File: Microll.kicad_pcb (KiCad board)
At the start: 2 copper layers, 5 parts, among them J1 USB_C_Receptacle, U1 AP7173-FNG-7, U2 STM32G0B1CBU6, U3 ESP32-C3-WROOM-02-N4, U4 LSM6DSL

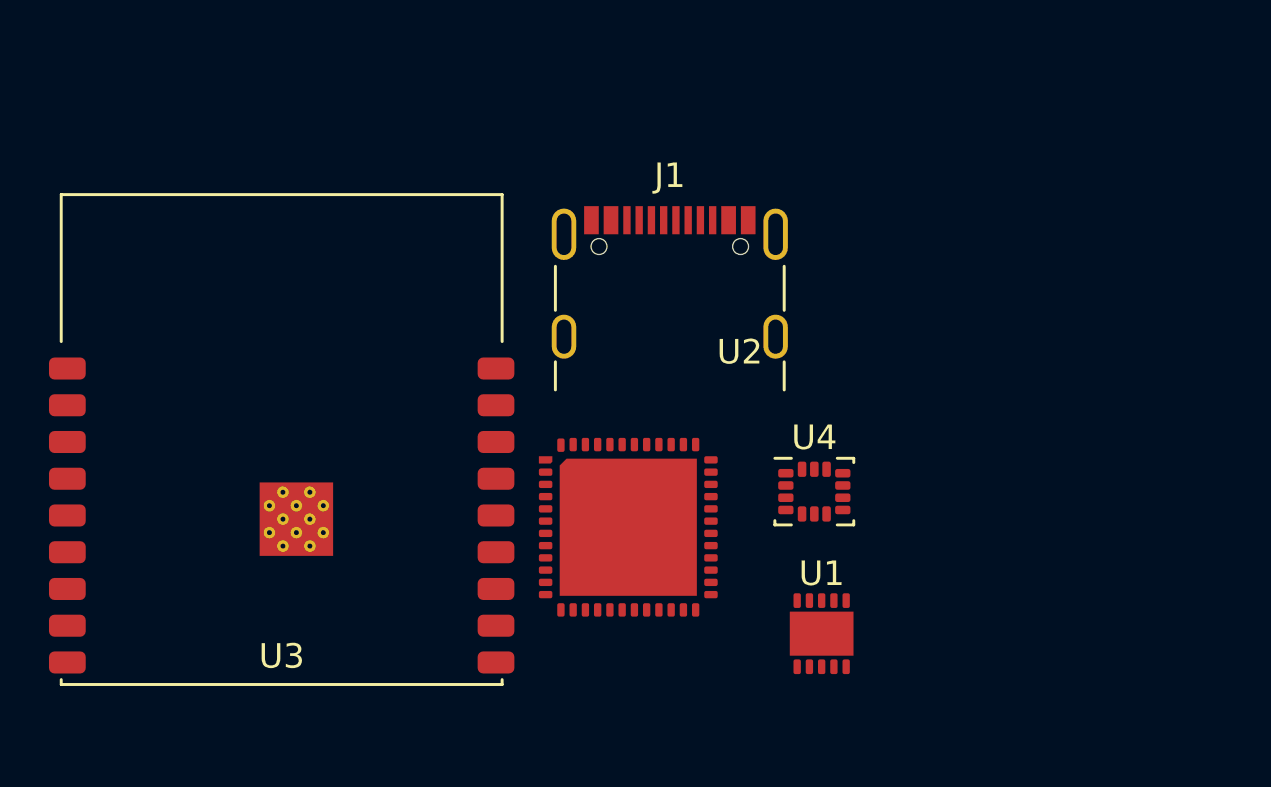
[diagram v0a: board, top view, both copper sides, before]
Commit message: Added 3D models to all PCB components. Added switch for USB programming between microcontrollers
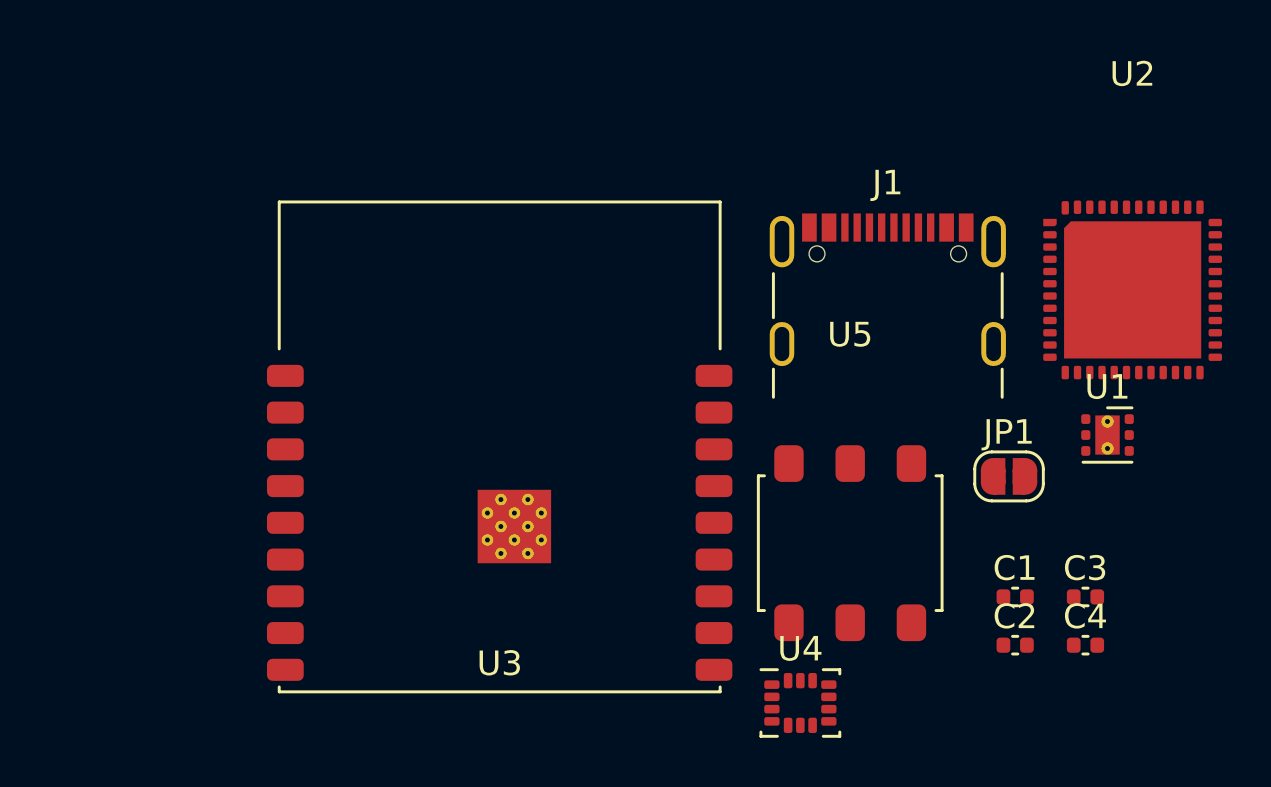
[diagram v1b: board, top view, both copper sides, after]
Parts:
- added C1: 1uF, Capacitor_SMD:C_0402_1005Metric, F.Cu at (159.2, 94.4)
- added C2: 1uF, Capacitor_SMD:C_0402_1005Metric, F.Cu at (159.2, 96.4)
- added C3: 100nF, Capacitor_SMD:C_0402_1005Metric, F.Cu at (162.1, 94.4)
- added C4: 100nF, Capacitor_SMD:C_0402_1005Metric, F.Cu at (162.1, 96.4)
- added JP1: SolderJumper_2_Open, Jumper:SolderJumper-2_P1.3mm_Open_RoundedPad1.0x1.5mm, F.Cu at (158.9, 89.5)
- added U5: DPDT_Switch_x2, DPDT_Switch_x2:DPDT_Switch_x2, F.Cu at (152.5, 92.2)
- U1: value AP7173-FNG-7 -> TLV76733DRVx; footprint AP7173-FNG-7:AP7173-FNG-7 -> Package_SON:WSON-6-1EP_2x2mm_P0.65mm_EP1x1.6mm_ThermalVias
- moved U2 17.5 mm to (164.0, 81.9)
- moved U1 14.2 mm to (163.0, 87.8)
- moved J1 8.91 mm to (154.0, 83.0)
- moved U3 8.91 mm to (138.2, 91.4)
- moved U4 8.65 mm to (150.4, 98.7)
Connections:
- J1 pad A1: Net-(J1-PadA1) -> GND
- J1 pad A12: Net-(J1-PadA1) -> GND
- J1 pad A4: Net-(J1-PadA4) -> +5V
- J1 pad A6: unconnected-(J1-PadA6) -> Net-(J1-PadA6)
- J1 pad A7: unconnected-(J1-PadA7) -> Net-(J1-PadA7)
- J1 pad A9: Net-(J1-PadA4) -> +5V
- J1 pad B1: Net-(J1-PadA1) -> GND
- J1 pad B12: Net-(J1-PadA1) -> GND
- J1 pad B4: Net-(J1-PadA4) -> +5V
- J1 pad B6: unconnected-(J1-PadB6) -> Net-(J1-PadA6)
- J1 pad B7: unconnected-(J1-PadB7) -> Net-(J1-PadA7)
- J1 pad B9: Net-(J1-PadA4) -> +5V
- U1 pad 1: unconnected-(U1-Pad1) -> +3.3V
- U1 pad 2: unconnected-(U1-Pad2) -> Net-(C2-Pad2)
- U1 pad 3: unconnected-(U1-Pad3) -> Net-(C1-Pad2)
- U1 pad 4: unconnected-(U1-Pad4) -> +5V
- U1 pad 5: unconnected-(U1-Pad5) -> Net-(C1-Pad2)
- U1 pad 6: unconnected-(U1-Pad6) -> +5V
- U1 pad 7: unconnected-(U1-Pad7) -> Net-(C1-Pad2)
- U2 pad 33: unconnected-(U2-Pad33) -> /STM32_USB-
- U2 pad 34: unconnected-(U2-Pad34) -> /STM32_USB+
- U3 pad 13: unconnected-(U3-Pad13) -> /ESP32_USB-
- U3 pad 14: unconnected-(U3-Pad14) -> /ESP32_USB+
- U4 pad 5: unconnected-(U4-Pad5) -> Net-(U4-Pad5)
- U4 pad 6: unconnected-(U4-Pad6) -> GND
- U4 pad 7: unconnected-(U4-Pad7) -> GND
- U4 pad 8: unconnected-(U4-Pad8) -> Net-(U4-Pad8)

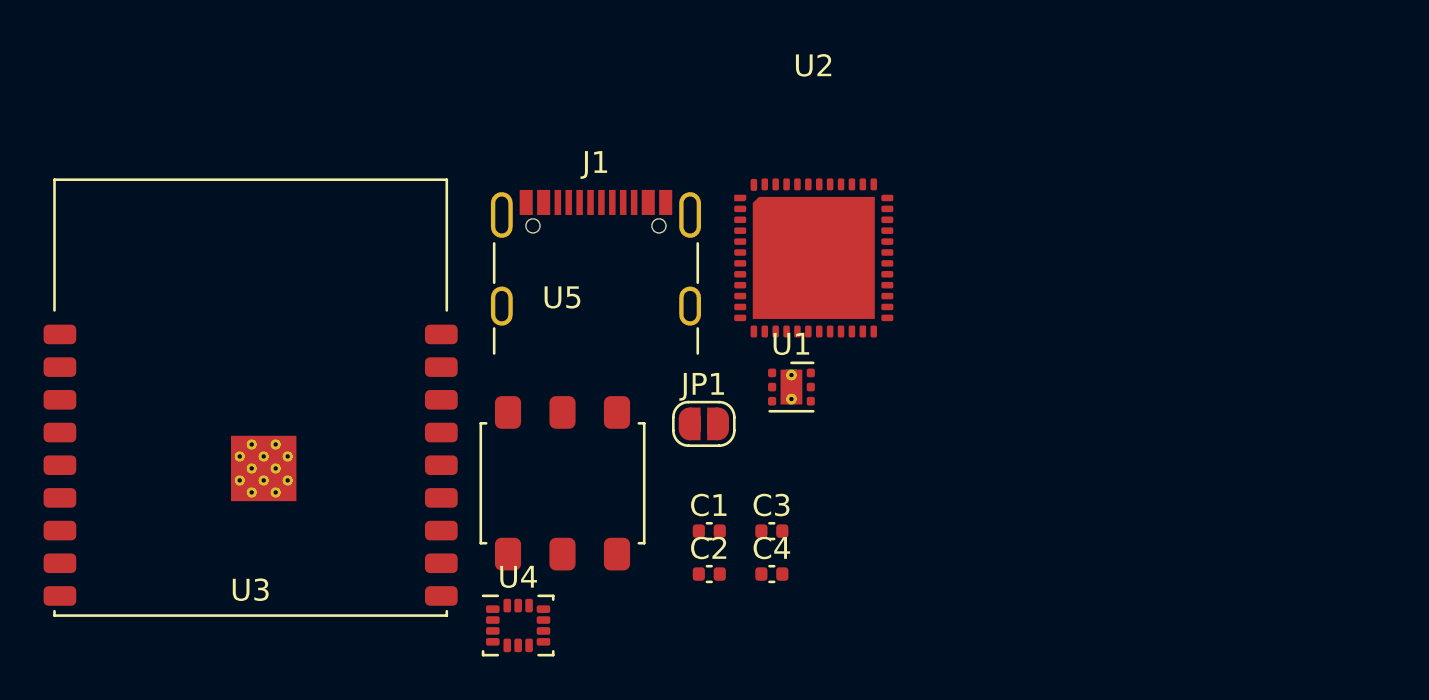
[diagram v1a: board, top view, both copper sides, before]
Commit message: Added ESD protection, decoupling capacitors and new footprints
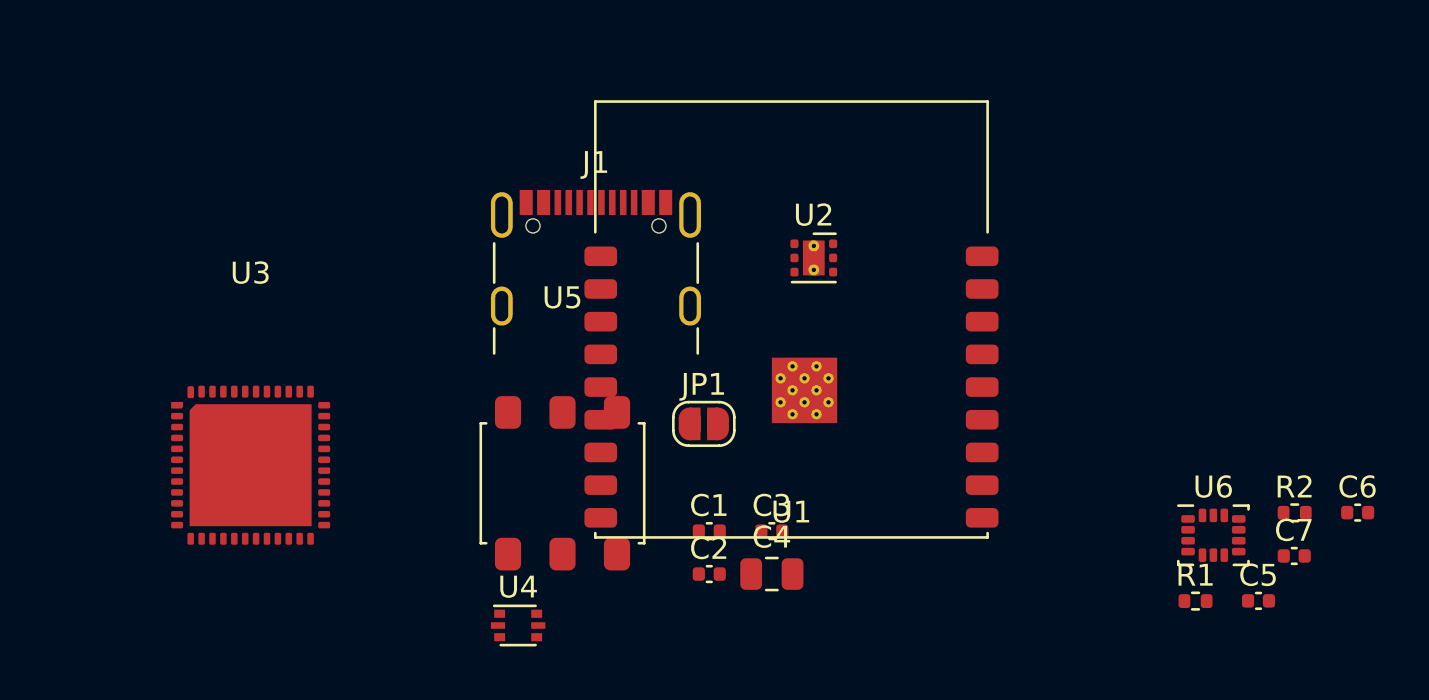
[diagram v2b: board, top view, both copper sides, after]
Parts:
- added C5: 100nF, Capacitor_SMD:C_0402_1005Metric, F.Cu at (184.4, 97.6)
- added C6: 100nF, Capacitor_SMD:C_0402_1005Metric, F.Cu at (188.9, 93.5)
- added C7: 100nF, Capacitor_SMD:C_0402_1005Metric, F.Cu at (186.0, 95.5)
- added R1: 10k, Resistor_SMD:R_0402_1005Metric, F.Cu at (181.5, 97.6)
- added R2: 10k, Resistor_SMD:R_0402_1005Metric, F.Cu at (186.1, 93.6)
- added U6: LSM6DSL, Package_LGA:LGA-14_3x2.5mm_P0.5mm_LayoutBorder3x4y, F.Cu at (182.3, 94.6)
- C4: value 100nF -> 4.7uF; footprint Capacitor_SMD:C_0402_1005Metric -> Capacitor_SMD:C_0805_2012Metric
- U1: value TLV76733DRVx -> ESP32-C3-WROOM-02-N4; footprint Package_SON:WSON-6-1EP_2x2mm_P0.65mm_EP1x1.6mm_ThermalVias -> ESP32:ESP32-C3-WROOM-02-N4
- U2: value STM32G0B1CBU6 -> TLV76733DRVx; footprint STM32:STM32G0B1CBU6 -> Package_SON:WSON-6-1EP_2x2mm_P0.65mm_EP1x1.6mm_ThermalVias
- U3: value ESP32-C3-WROOM-02-N4 -> STM32G0B1CBU6; footprint ESP32:ESP32-C3-WROOM-02-N4 -> STM32:STM32G0B1CBU6
- U4: value LSM6DSL -> USBLC6-2P6; footprint Package_LGA:LGA-14_3x2.5mm_P0.5mm_LayoutBorder3x4y -> Package_TO_SOT_SMD:SOT-666
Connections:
- C1 pad 2: Net-(C1-Pad2) -> GND
- C3 pad 1: Net-(U4-Pad5) -> +3.3V
- C4 pad 1: Net-(U4-Pad8) -> +3.3V
- J1 pad A6: Net-(J1-PadA6) -> /D+
- J1 pad A7: Net-(J1-PadA7) -> /D-
- J1 pad B6: Net-(J1-PadA6) -> /D+
- J1 pad B7: Net-(J1-PadA7) -> /D-
- U1 pad 2: Net-(C2-Pad2) -> unconnected-(U1-Pad2)
- U1 pad 3: Net-(C1-Pad2) -> (no net)
- U1 pad 4: +5V -> SCL
- U1 pad 5: Net-(C1-Pad2) -> unconnected-(U1-Pad5)
- U1 pad 6: +5V -> unconnected-(U1-Pad6)
- U1 pad 7: Net-(C1-Pad2) -> unconnected-(U1-Pad7)
- U2 pad 1: unconnected-(U2-Pad1) -> +3.3V
- U2 pad 2: unconnected-(U2-Pad2) -> Net-(C2-Pad2)
- U2 pad 3: unconnected-(U2-Pad3) -> GND
- U2 pad 4: unconnected-(U2-Pad4) -> +5V
- U2 pad 5: unconnected-(U2-Pad5) -> GND
- U2 pad 6: unconnected-(U2-Pad6) -> +5V
- U2 pad 7: unconnected-(U2-Pad7) -> GND
- U3 pad 11: unconnected-(U3-Pad11) -> /ADC1_IN0
- U3 pad 12: unconnected-(U3-Pad12) -> /ADC1_IN1
- U3 pad 13: /ESP32_USB- -> unconnected-(U3-Pad13)
- U3 pad 14: /ESP32_USB+ -> unconnected-(U3-Pad14)
- U3 pad 15: unconnected-(U3-Pad15) -> /DAC1_OUT1
- U3 pad 16: unconnected-(U3-Pad16) -> SPI_SCK
- U3 pad 17: unconnected-(U3-Pad17) -> SPI_MISO
- U3 pad 18: unconnected-(U3-Pad18) -> SPI_MOSI
- U3 pad 3: (no net) -> unconnected-(U3-Pad3)
- U3 pad 5: unconnected-(U3-Pad5) -> +3.3V
- U3 pad 6: unconnected-(U3-Pad6) -> +3.3V
- U3 pad 7: unconnected-(U3-Pad7) -> GND
- U4 pad 1: unconnected-(U4-Pad1) -> /USB-
- U4 pad 2: unconnected-(U4-Pad2) -> GND
- U4 pad 3: unconnected-(U4-Pad3) -> /USB+
- U4 pad 4: unconnected-(U4-Pad4) -> /D+
- U4 pad 5: Net-(U4-Pad5) -> +5V
- U4 pad 6: GND -> /D-
- U5 pad 1: /STM32_USB+ -> STM32_USB+
- U5 pad 2: Net-(J1-PadA7) -> /USB+
- U5 pad 3: /STM32_USB- -> ESP32_USB+
- U5 pad 4: /ESP32_USB+ -> STM32_USB-
- U5 pad 5: Net-(J1-PadA6) -> /USB-
- U5 pad 6: /ESP32_USB- -> ESP32_USB-

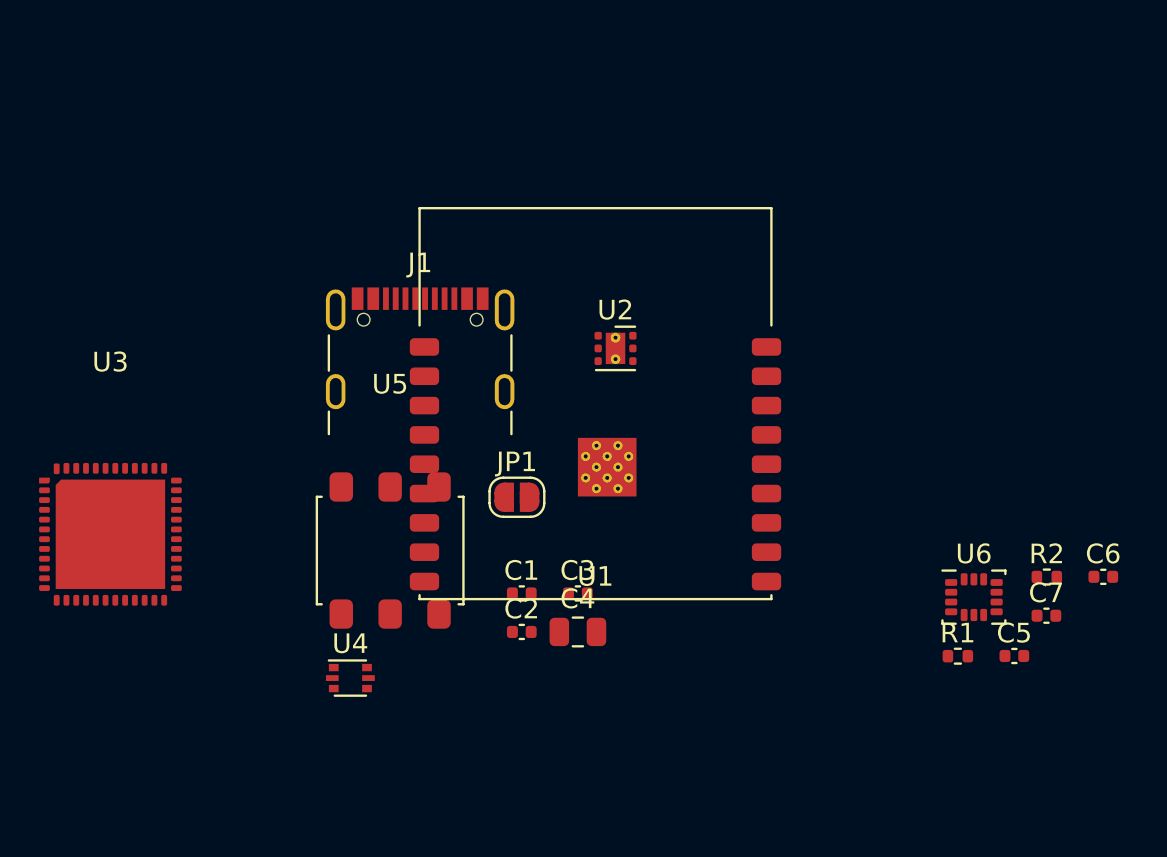
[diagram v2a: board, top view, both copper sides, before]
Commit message: Added nets to the LEDs. Pretty much all that is left in the scematic is adding the I/O pins and then it's off to the PCB layout
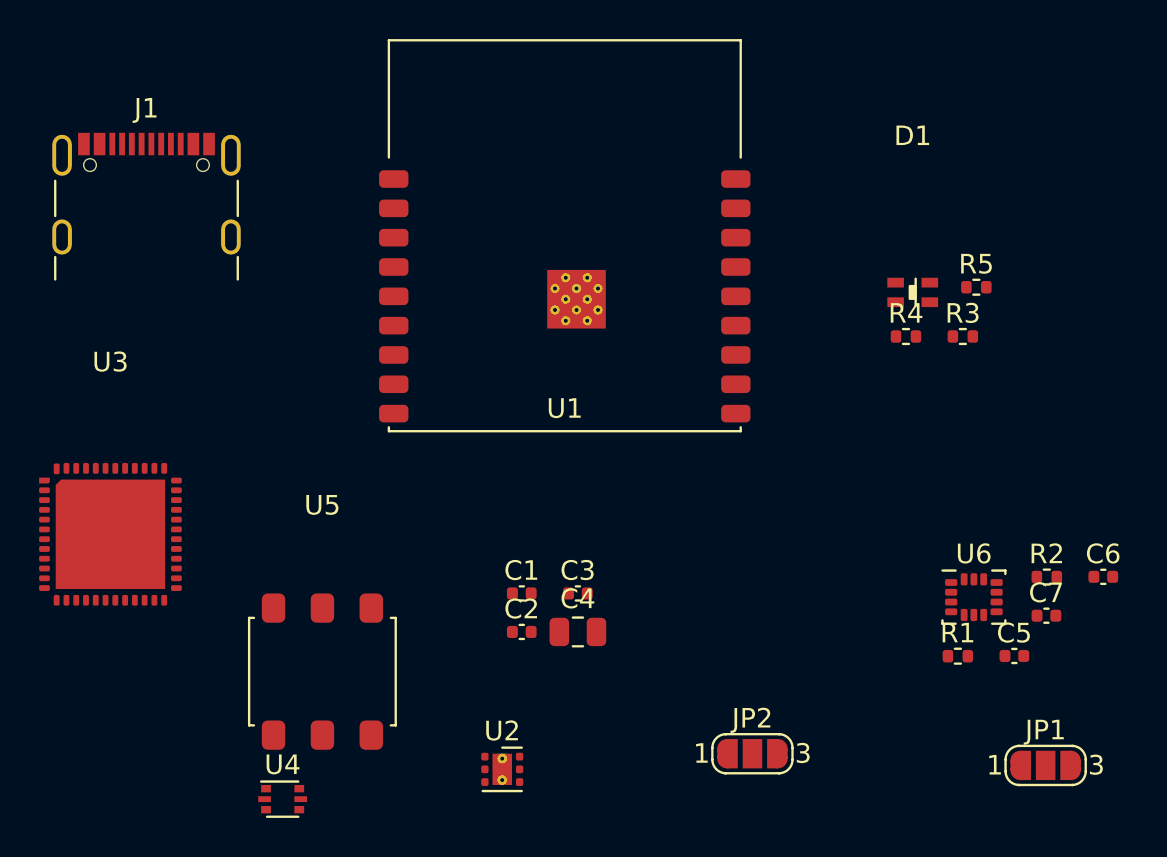
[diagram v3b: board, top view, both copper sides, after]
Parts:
- added D1: LED_ARGB, RGB_LED:APTF1616LSEEZGKQBKC, F.Cu at (179.2, 79.0)
- added JP2: SolderJumper_3_Open, Jumper:SolderJumper-3_P1.3mm_Open_RoundedPad1.0x1.5mm_NumberLabels, F.Cu at (171.0, 102.6)
- added R3: 10k, Resistor_SMD:R_0402_1005Metric, F.Cu at (181.8, 81.3)
- added R4: 10k, Resistor_SMD:R_0402_1005Metric, F.Cu at (178.9, 81.3)
- added R5: 10k, Resistor_SMD:R_0402_1005Metric, F.Cu at (182.5, 78.7)
- JP1: value SolderJumper_2_Open -> SolderJumper_3_Open; footprint Jumper:SolderJumper-2_P1.3mm_Open_RoundedPad1.0x1.5mm -> Jumper:SolderJumper-3_P1.3mm_Open_RoundedPad1.0x1.5mm_NumberLabels
- moved JP1 30.3 mm to (186.0, 103.2)
- moved U2 22.3 mm to (158.2, 103.4)
- moved J1 16.1 mm to (140.0, 75.1)
- moved U1 8.73 mm to (161.4, 79.2)
- moved U5 7.10 mm to (149.0, 98.4)
- moved U4 7.10 mm to (147.0, 104.9)
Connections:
- JP1 pad 1: unconnected-(JP1-Pad1) -> +3.3V
- JP1 pad 2: unconnected-(JP1-Pad2) -> Net-(JP1-Pad2)
- R1 pad 1: +3.3V -> Net-(D1-Pad2)
- R1 pad 2: SDA -> /Red
- R2 pad 1: +3.3V -> Net-(D1-Pad3)
- R2 pad 2: SCL -> /Green
- U1 pad 2: unconnected-(U1-Pad2) -> Net-(JP1-Pad2)
- U3 pad 1: unconnected-(U3-Pad1) -> /Red
- U3 pad 2: unconnected-(U3-Pad2) -> /Green
- U3 pad 3: unconnected-(U3-Pad3) -> /Blue
